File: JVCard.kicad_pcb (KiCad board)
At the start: 2 copper layers, 170 x 130 mm, 75 parts, among them J6 Conn_02x25_Odd_Even, Q1 mmbt3904, Q2 mmbt3904, Q3 mmbt3904, Q4 mmbt3904, Q5 mmbt3904, Q6 mmbt3904, U1 AMS1117-5.0, U4 SCART_CONN

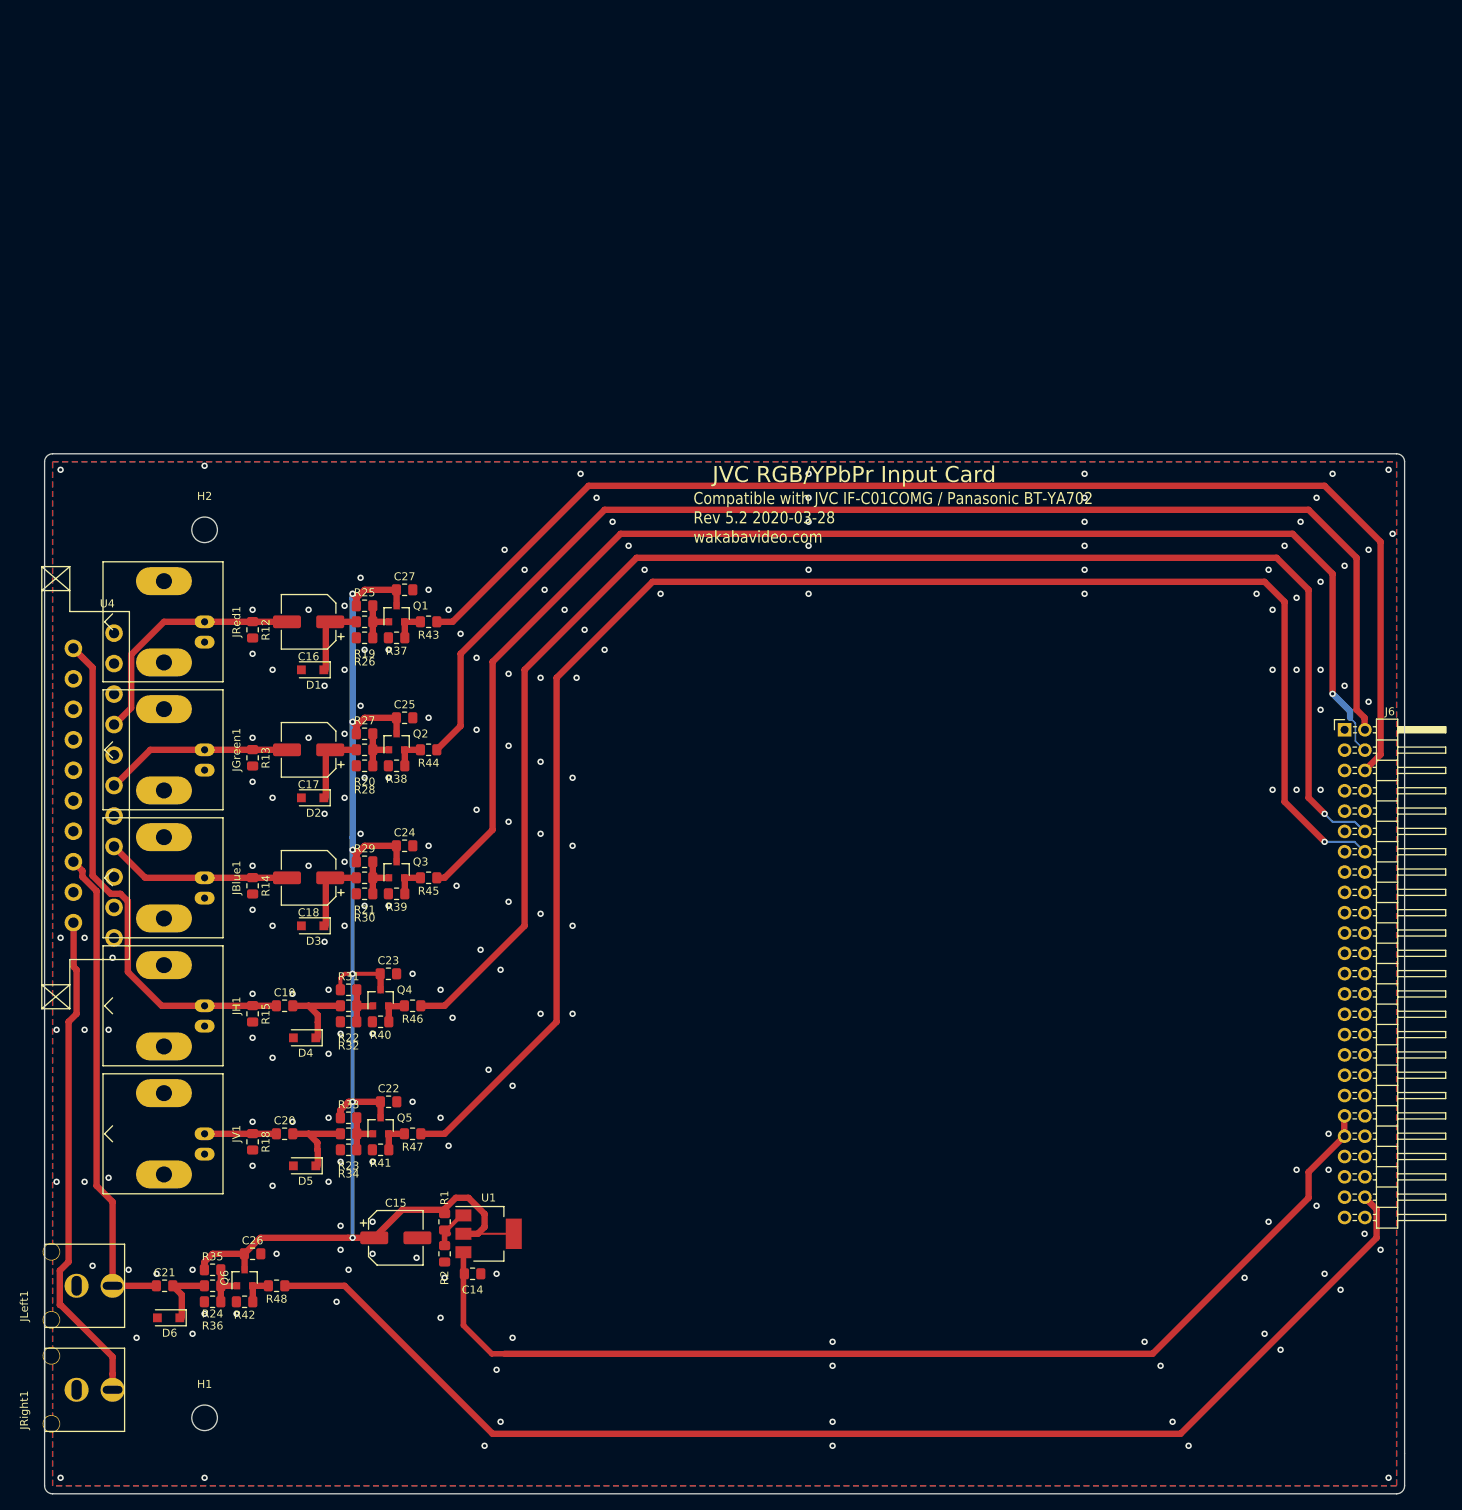
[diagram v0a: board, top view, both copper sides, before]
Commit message: draft scart-vga inside
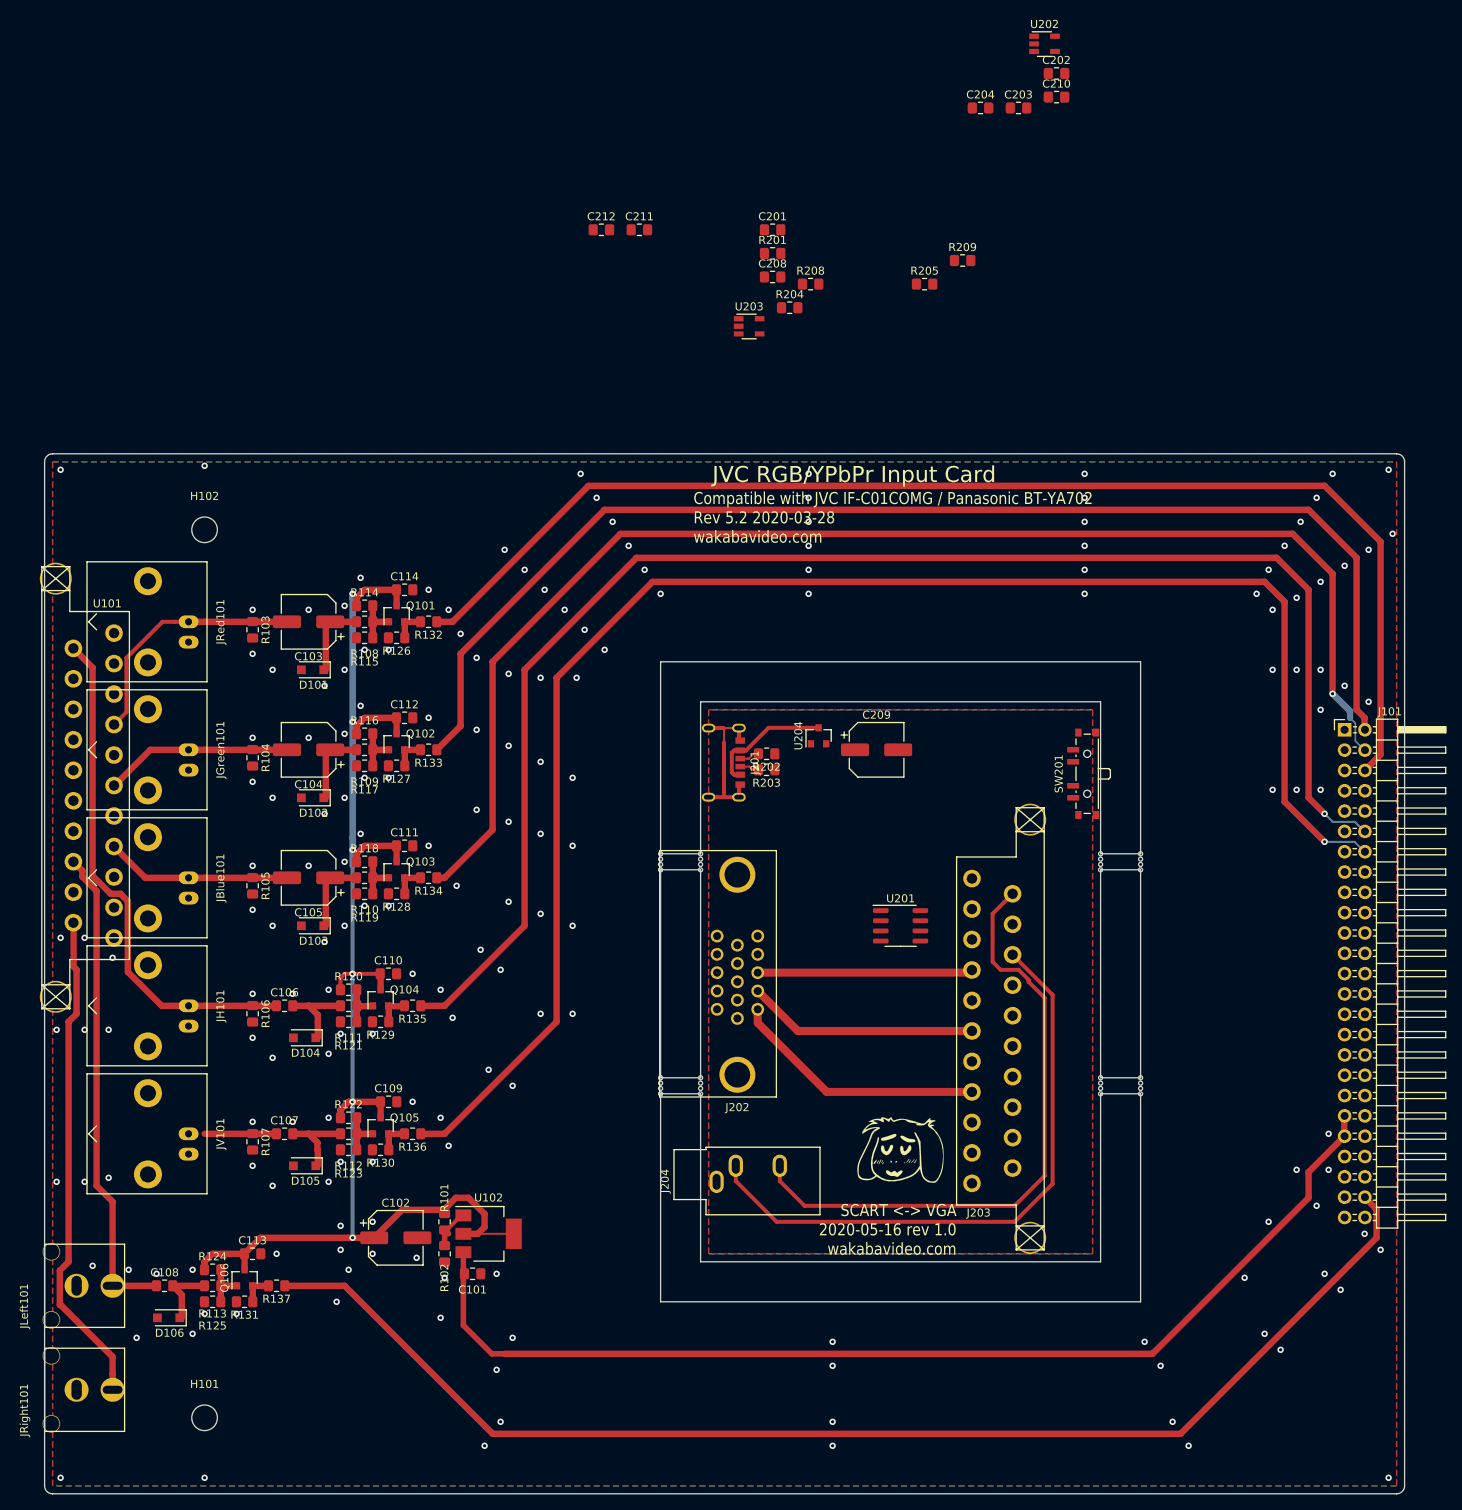
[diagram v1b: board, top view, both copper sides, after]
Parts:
- added C201: 100n, Capacitor_SMD:C_0805_2012Metric_Pad1.15x1.40mm_HandSolder, F.Cu at (31.0, -18.0)
- added C202: 100n, Capacitor_SMD:C_0805_2012Metric_Pad1.15x1.40mm_HandSolder, F.Cu at (66.5, -37.5)
- added C203: 100n, Capacitor_SMD:C_0805_2012Metric_Pad1.15x1.40mm_HandSolder, F.Cu at (61.7, -33.2)
- added C204: 100n, Capacitor_SMD:C_0805_2012Metric_Pad1.15x1.40mm_HandSolder, F.Cu at (57.0, -33.2)
- added C208: 100n, Capacitor_SMD:C_0805_2012Metric_Pad1.15x1.40mm_HandSolder, F.Cu at (31.0, -12.1)
- added C209: 33u, Capacitor_SMD:CP_Elec_6.3x7.7, F.Cu at (44.0, 47.0)
- added C210: 10u, Capacitor_SMD:C_0805_2012Metric_Pad1.15x1.40mm_HandSolder, F.Cu at (66.5, -34.6)
- added C211: 100n, Capacitor_SMD:C_0805_2012Metric_Pad1.15x1.40mm_HandSolder, F.Cu at (14.3, -18.0)
- added C212: 100n, Capacitor_SMD:C_0805_2012Metric_Pad1.15x1.40mm_HandSolder, F.Cu at (9.60, -18.0)
- added GOTE201: Fiducial, videobits:uwuriel, F.Cu at (47.0, 97.0)
- added H201: MountingHole, videobits:mousebite, F.Cu at (72.0, 60.0)
- added H202: MountingHole, videobits:mousebite, F.Cu at (77.0, 60.0)
- added H203: MountingHole, videobits:mousebite, F.Cu at (77.0, 88.0)
- added H204: MountingHole, videobits:mousebite, F.Cu at (72.0, 88.0)
- added H205: MountingHole, videobits:mousebite, F.Cu at (17.0, 60.0)
- added H206: MountingHole, videobits:mousebite, F.Cu at (17.0, 88.0)
- added H207: MountingHole, videobits:mousebite, F.Cu at (22.0, 88.0)
- added H208: MountingHole, videobits:mousebite, F.Cu at (22.0, 60.0)
- added J201: USB_C_Receptacle_Power, videobits:USB_C_Receptacle_Generic_Power_Only, F.Cu at (20.4, 48.6)
- added J202: VGA, custom_components:VGA_CONN, F.Cu at (26.6, 76.0)
- added J203: SCART_CONN, custom_components:SCART_CONN, F.Cu at (61.0, 65.0)
- added J204: AudioJack3, Connector_Audio:Jack_3.5mm_CUI_SJ1-3533NG_Horizontal, F.Cu at (24.0, 101.0)
- added R201: 75, Resistor_SMD:R_0805_2012Metric_Pad1.15x1.40mm_HandSolder, F.Cu at (31.0, -15.1)
- added R202: 5k1, Resistor_SMD:R_0805_2012Metric_Pad1.15x1.40mm_HandSolder, F.Cu at (30.2, 47.5)
- added R203: 5k1, Resistor_SMD:R_0805_2012Metric_Pad1.15x1.40mm_HandSolder, F.Cu at (30.2, 49.5)
- added R204: 680k, Resistor_SMD:R_0805_2012Metric_Pad1.15x1.40mm_HandSolder, F.Cu at (33.1, -8.26)
- added R205: 1k, Resistor_SMD:R_0805_2012Metric_Pad1.15x1.40mm_HandSolder, F.Cu at (50.0, -11.2)
- added R208: 1k, Resistor_SMD:R_0805_2012Metric_Pad1.15x1.40mm_HandSolder, F.Cu at (35.8, -11.2)
- added R209: 1k33, Resistor_SMD:R_0805_2012Metric_Pad1.15x1.40mm_HandSolder, F.Cu at (54.8, -14.2)
- added SW201: SW_SP3T, Button_Switch_SMD:SW_SP3T_PCM13, F.Cu at (70.0, 50.0)
- added U201: LM1881, Package_SO:SOIC-8_3.9x4.9mm_P1.27mm, F.Cu at (47.0, 69.0)
- added U202: 74AHC1G86, Package_TO_SOT_SMD:TSOT-23-5, F.Cu at (65.0, -41.2)
- added U203: 74AHC1G86, Package_TO_SOT_SMD:TSOT-23-5, F.Cu at (28.1, -5.94)
- added U204: SC6206B-65K5, Package_TO_SOT_SMD:SOT-23, F.Cu at (36.8, 45.2)
- JBlue101: renamed from JBlue1; footprint Connector_Coaxial:BNC_Amphenol_B6252HB-NPP3G-50_Horizontal -> videobits:BNC_Amphenol_B6252HB-NPP3G-50_Horizontal_smallerpads
- JGreen101: renamed from JGreen1; footprint Connector_Coaxial:BNC_Amphenol_B6252HB-NPP3G-50_Horizontal -> videobits:BNC_Amphenol_B6252HB-NPP3G-50_Horizontal_smallerpads
- JH101: renamed from JH1; footprint Connector_Coaxial:BNC_Amphenol_B6252HB-NPP3G-50_Horizontal -> videobits:BNC_Amphenol_B6252HB-NPP3G-50_Horizontal_smallerpads
- JRed101: renamed from JRed1; footprint Connector_Coaxial:BNC_Amphenol_B6252HB-NPP3G-50_Horizontal -> videobits:BNC_Amphenol_B6252HB-NPP3G-50_Horizontal_smallerpads
- JV101: renamed from JV1; footprint Connector_Coaxial:BNC_Amphenol_B6252HB-NPP3G-50_Horizontal -> videobits:BNC_Amphenol_B6252HB-NPP3G-50_Horizontal_smallerpads
- R102: renamed from R2; value 4k8 -> 1k
- moved JBlue101 2.00 mm to (-42.0, 63.0)
- moved JGreen101 2.00 mm to (-42.0, 47.0)
- moved JH101 2.00 mm to (-42.0, 79.0)
- moved JRed101 2.00 mm to (-42.0, 31.0)
- moved JV101 2.00 mm to (-42.0, 95.0)
- renumbered C14 to C101, C15 to C102, C16 to C103, C17 to C104, C18 to C105, C19 to C106, C20 to C107, C21 to C108, C22 to C109, C23 to C110, C24 to C111, C25 to C112, C26 to C113, C27 to C114, D1 to D101, D2 to D102, D3 to D103, D4 to D104, D5 to D105, D6 to D106, H1 to H101, H2 to H102, J6 to J101, JLeft1 to JLeft101, JRight1 to JRight101, Q1 to Q101, Q2 to Q102, Q3 to Q103, Q4 to Q104, Q5 to Q105, Q6 to Q106, R1 to R101, R12 to R103, R13 to R104, R14 to R105, R15 to R106, R18 to R107, R19 to R108, R20 to R109, R21 to R110, R22 to R111, R23 to R112, R24 to R113, R25 to R114, R26 to R115, R27 to R116, R28 to R117, R29 to R118, R30 to R119, R31 to R120, R32 to R121, R33 to R122, R34 to R123, R35 to R124, R36 to R125, R37 to R126, R38 to R127, R39 to R128, R40 to R129, R41 to R130, R42 to R131, R43 to R132, R44 to R133, R45 to R134, R46 to R135, R47 to R136, R48 to R137, U4 to U101, U1 to U102
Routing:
- net Net-(J203-Pad2): track 0.00 -> 78.1 mm
- net Net-(J203-Pad6): track 0.00 -> 76.3 mm
- net /VGASCART/Red: track 0.00 -> 32.1 mm
- net /VGASCART/Green: track 0.00 -> 28.8 mm
- net /VGASCART/Blue: track 0.00 -> 26.9 mm
- net GND: track 0.00 -> 19.5 mm
- net +5V: track 0.00 -> 15.7 mm
- net Net-(J201-PadB5): track 0.00 -> 3.01 mm
- net Net-(J201-PadA5): track 0.00 -> 2.52 mm
- added copper zone on B.Cu, net GND
- added copper zone on F.Cu, net GND
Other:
- outline, holes or cut-outs redrawn
- board text added: "SCART <-> VGA 2020-05-16 rev 1.0 wakabavideo.com"
